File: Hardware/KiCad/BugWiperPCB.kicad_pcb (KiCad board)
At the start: 2 copper layers, 110 x 40 mm, 88 parts, among them J1 UJ20-C-H-G-SMT-1-P16-TR, J2 TBLH10-350-06BK, J3 Phoenix_1776508, J4 RJ45, J5 Conn_TagConnect_TC2030-NL_ESP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, Q1 NMOS_SO-8, U1 ESP32-S3-WROOM-1, U2 BTN9960LV, U3 BTN9960LV, U4 INA180A2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

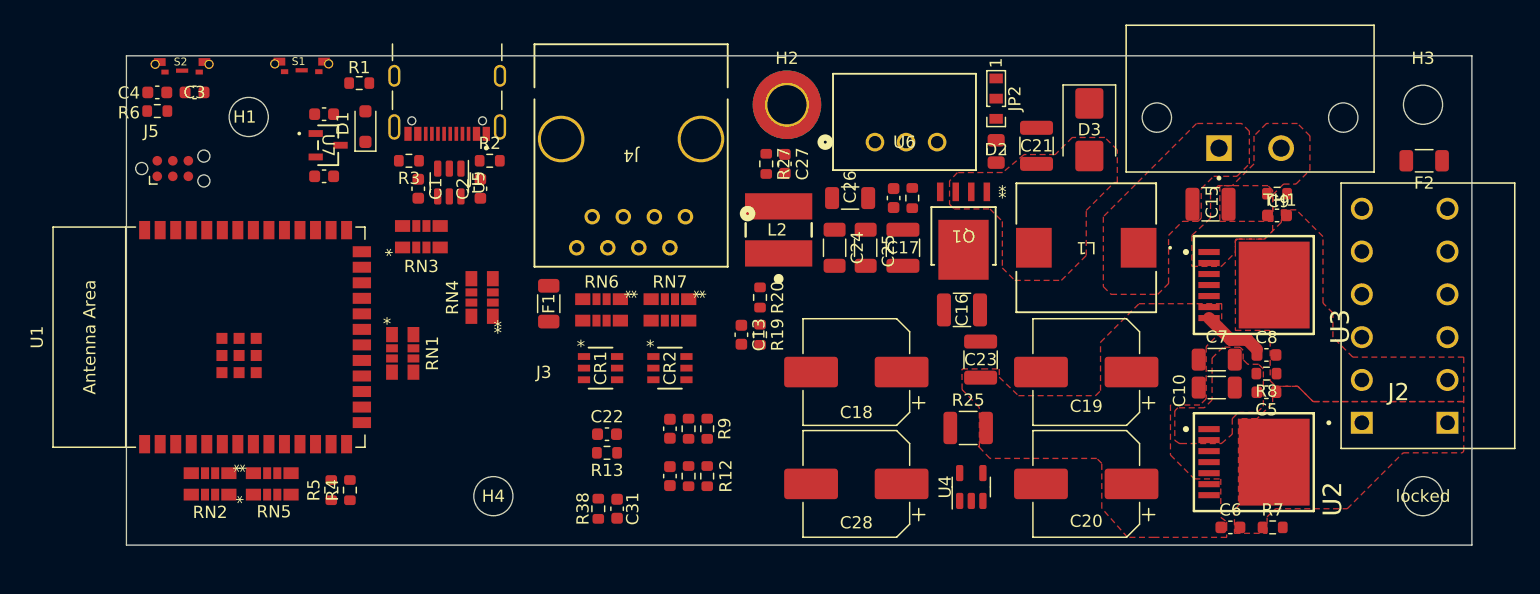
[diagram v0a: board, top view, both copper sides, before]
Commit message: update PCB, routing and Connector
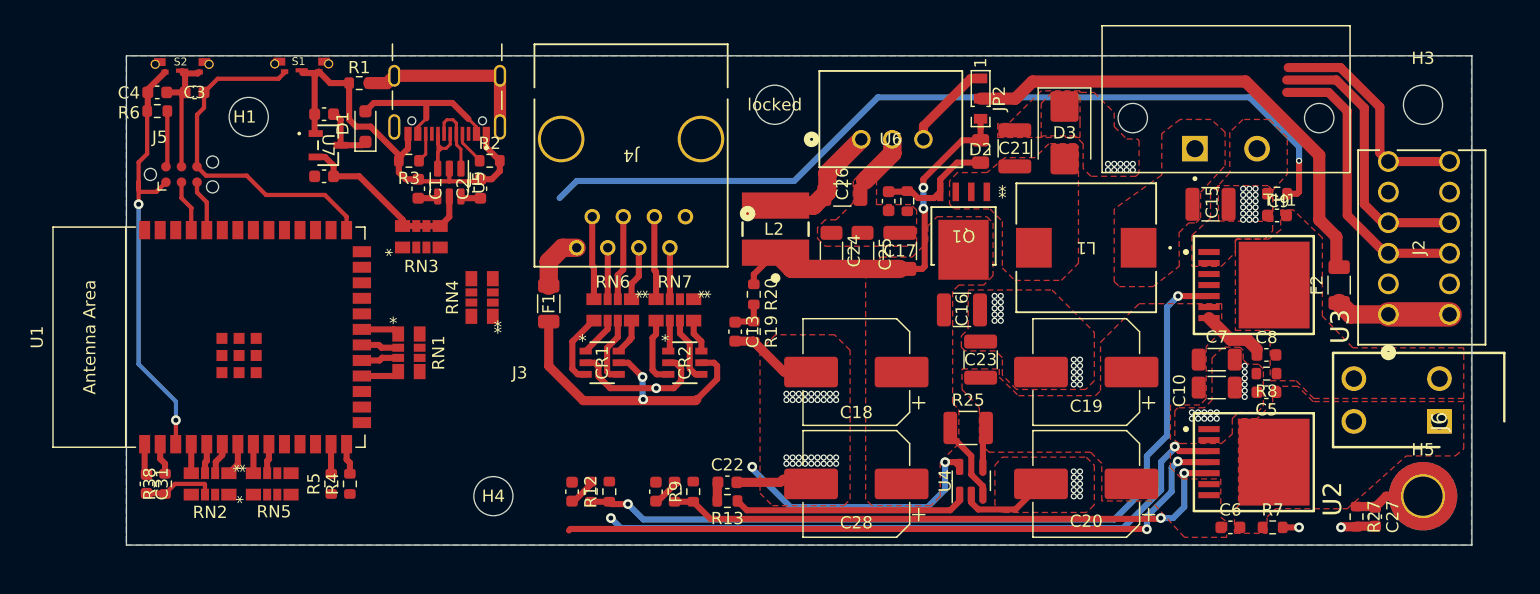
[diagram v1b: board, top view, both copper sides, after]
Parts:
- added J6: 1824420000, BugWiper_lib:SHDR4W80P700X350_2X2_770X1400X850P, F.Cu at (217.3, 89.9)
- J2: value TBLH10-350-06BK -> 1770924; footprint TBLH10_350_06BK-2:CUI_TBLH10-350-06BK -> BugWiper_lib:CONN_1814537
- moved locked 61.9 mm to (163.0, 64.0)
- moved H5 61.1 mm to (216.0, 96.0)
- moved C27 56.2 mm to (212.1, 97.7)
- moved R27 56.2 mm to (210.6, 97.7)
- moved C31 38.5 mm to (111.6, 95.0)
- moved R38 35.5 mm to (113.2, 95.0)
- moved J2 21.1 mm to (218.2, 70.2)
- moved F2 12.3 mm to (209.1, 78.7), turned to 90 degrees
- moved C22 10.6 mm to (159.1, 94.9)
- moved R13 10.6 mm to (159.1, 96.4)
- moved C12 8.10 mm to (146.4, 95.6)
- moved R11 8.10 mm to (148.0, 95.6), turned to -90 degrees
- moved R12 8.10 mm to (149.5, 95.6), turned to 90 degrees
- moved C11 5.27 mm to (153.3, 95.6)
- moved R10 5.27 mm to (154.8, 95.6), turned to -90 degrees
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- renumbered H2 to H5
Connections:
- C5 pad 1: Motor+ -> /Power/Motor+
- C6 pad 2: Motor+ -> /Power/Motor+
- C8 pad 2: Motor- -> /Power/Motor-
- C9 pad 1: Motor- -> /Power/Motor-
- F2 pad 1: Net-(J2-3) -> Net-(F2-Pad1)
- R7 pad 1: Motor+ -> /Power/Motor+
- R8 pad 1: Motor- -> /Power/Motor-
- RN1 pad 1: /ESP32-S3/M_IHN2 -> M__INH2
- RN1 pad 2: /ESP32-S3/M_INH1 -> M__INH1
- RN1 pad 3: /ESP32-S3/M_IN2 -> M__IN2
- RN1 pad 4: /ESP32-S3/M_IN1 -> M__IN1
- RN1 pad 5: M__IN1 -> /ESP32-S3/M_IN1
- RN1 pad 6: M__IN2 -> /ESP32-S3/M_IN2
- RN1 pad 7: M__INH1 -> /ESP32-S3/M_INH1
- RN1 pad 8: M__INH2 -> /ESP32-S3/M_IHN2
- U2 pad 8: Motor+ -> /Power/Motor+
- U3 pad 8: Motor- -> /Power/Motor-
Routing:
- net GND: track 0.00 -> 89.3 mm, vias 0 -> 113
- net +3.3V: track 0.00 -> 78.3 mm, vias 0 -> 4
- net /ESP32-S3/ADC_NTC: track 0.00 -> 76.3 mm, vias 0 -> 1
- net Net-(U3-IS): track 0.00 -> 66.4 mm, vias 0 -> 2
- net /ESP32-S3/M_INH1: track 0.00 -> 56.5 mm, vias 0 -> 2
- net /ESP32-S3/M_IN1: track 0.00 -> 53.6 mm, vias 0 -> 2
- net Net-(U2-IS): track 0.00 -> 47.4 mm, vias 0 -> 2
- net Net-(JP2-C): track 0.00 -> 40.7 mm
- net +12V: track 0.00 -> 38.1 mm, vias 0 -> 2
- net EN: track 0.00 -> 35.9 mm, vias 0 -> 2
- net Boot: track 0.00 -> 28.7 mm
- net EN_C2: track 0.00 -> 23.8 mm
- net EN_C1: track 0.00 -> 22.8 mm
- net /ESP32-S3/ADC_INA: track 0.00 -> 18.8 mm
- net switsch: track 0.00 -> 18.6 mm
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- added copper zone on F.Cu, net +12V
- added copper zone on F.Cu, net /Power/Motor+
- added copper zone on F.Cu, net /Power/Motor-
- added copper zone on B.Cu, net GND
- removed copper zone on F.Cu, net Motor+
- removed copper zone on F.Cu, net Motor-

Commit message: update PCB
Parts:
- U1: footprint PCM_Espressif:ESP32-S3-WROOM-1 -> BugWiper_lib:ESP32-S3-WROOM-1

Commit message: turn the esp32 90°
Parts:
- removed RN3: 47k_Pack04, BugWiper_lib:BO_CAY16
- moved C29 35.3 mm to (154.5, 90.9), turned to -90 degrees
- moved C30 35.0 mm to (149.5, 90.9), turned to -90 degrees
- moved U7 34.5 mm to (152.0, 90.6), turned to 0 degrees
- moved C31 27.9 mm to (139.3, 92.0), turned to 180 degrees
- moved H4 26.7 mm to (114.0, 90.0)
- moved R38 26.6 mm to (139.3, 90.5), turned to 0 degrees
- moved R5 24.1 mm to (140.0, 74.8), turned to -90 degrees
- moved RN2 23.9 mm to (139.3, 86.8), turned to 0 degrees
- moved R4 22.6 mm to (138.5, 74.8), turned to -90 degrees
- moved RN5 21.9 mm to (139.3, 81.7), turned to 180 degrees
- moved RN4 20.5 mm to (123.5, 66.5), turned to -90 degrees
- moved D1 15.2 mm to (141.8, 74.7)
- moved RN1 13.9 mm to (128.6, 71.1), turned to 90 degrees
- moved J5 11.9 mm to (113.7, 81.5), turned to 90 degrees
- moved C3 11.6 mm to (114.8, 74.6), turned to 90 degrees
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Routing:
- net +3.3V: track 78.3 -> 39.5 mm, vias 4 -> 3
- net EN: track 35.9 -> 3.75 mm, vias 2 -> 1
- net Boot: track 28.7 -> 0.00 mm
- net GND: track 89.3 -> 64.4 mm
- net Net-(D1-A): track 13.6 -> 8.29 mm
- net TX: track 4.26 -> 0.00 mm
- net RX: track 4.25 -> 0.00 mm
- net Net-(C1-Pad2): track 1.65 -> 5.84 mm
- net Net-(C2-Pad1): track 1.65 -> 4.04 mm
- net Net-(J1-SHIELD-PadSH1): track 15.1 -> 12.8 mm
- net +5V: track 4.99 -> 2.84 mm
- net D-: track 2.43 -> 4.38 mm
- net Net-(F1-Pad2): track 4.74 -> 3.43 mm
- net M__INH2: track 3.13 -> 2.59 mm
- net M__INH1: track 3.06 -> 2.53 mm
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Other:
- outline, holes or cut-outs redrawn

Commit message: routing
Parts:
- added C32: 10nF, Capacitor_SMD:C_0603_1608Metric, F.Cu at (124.7, 70.2)
- added C33: 10nF, Capacitor_SMD:C_0603_1608Metric, F.Cu at (124.7, 71.8)
- added C34: 10nF, Capacitor_SMD:C_0603_1608Metric, F.Cu at (120.3, 71.8)
- added C35: 10nF, Capacitor_SMD:C_0603_1608Metric, F.Cu at (120.3, 70.2)
- added C36: 10nF, Capacitor_SMD:C_0603_1608Metric, F.Cu at (141.0, 84.1)
- added C37: 10nF, Capacitor_SMD:C_0603_1608Metric, F.Cu at (138.4, 83.3)
- added C38: 10nF, Capacitor_SMD:C_0603_1608Metric, F.Cu at (154.7, 91.3)
- added R14: 1k, Resistor_SMD:R_0603_1608Metric, F.Cu at (142.6, 86.7)
- D1: value 1N5819WS -> locked
- moved TH1 26.9 mm to (209.0, 97.7), turned to -90 degrees
- moved C30 4.48 mm to (145.0, 90.2)
- moved C29 4.11 mm to (150.5, 90.2), turned to 90 degrees
- moved U7 3.74 mm to (148.3, 90.2)
- moved R19 3.08 mm to (158.7, 80.9), turned to 90 degrees
- moved R2 2.12 mm to (140.6, 70.9), turned to -90 degrees
- moved R3 2.12 mm to (132.5, 70.9), turned to -90 degrees
- moved RN5 1.83 mm to (141.0, 80.9)
- moved C13 1.73 mm to (160.3, 80.9), turned to 90 degrees
- moved R20 1.51 mm to (161.9, 80.9)
- moved S2 1.49 mm to (119.3, 60.0)
- moved RN4 1.42 mm to (122.6, 67.6)
- moved C16 0.91 mm to (178.1, 81.7)
- moved C23 0.77 mm to (180.0, 85.6)
- moved CR1 0.70 mm to (149.6, 85.1)
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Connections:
- net switsch renamed sw_1
- RN5 pad 3: unconnected-(RN5-R3.1-Pad3) -> Net-(RN5-R3.1)
- RN5 pad 6: unconnected-(RN5-R3.2-Pad6) -> SW1
- U1 pad 10: unconnected-(U1-GPIO17/U1TXD/ADC2_CH6-Pad10) -> SW1
- U1 pad 11: unconnected-(U1-GPIO18/U1RXD/ADC2_CH7/CLK_OUT3-Pad11) -> OUT1
- U1 pad 12: OUT1 -> OUT2
- U1 pad 17: OUT2 -> unconnected-(U1-GPIO9/TOUCH9/ADC1_CH8/FSPIHD/SUBSPIHD-Pad17)
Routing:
- net +3.3V: track 39.5 -> 166.5 mm, vias 3 -> 9
- net /ESP32-S3/M_IHN2: track 0.00 -> 86.9 mm, vias 0 -> 8
- net /ESP32-S3/M_IN2: track 0.00 -> 85.6 mm, vias 0 -> 6
- net EN_C2: track 23.8 -> 86.1 mm, vias 0 -> 8
- net EN_C1: track 22.8 -> 83.9 mm, vias 0 -> 4
- net EN: track 3.75 -> 58.5 mm, vias 1 -> 2
- net sw_1: track 18.6 -> 70.6 mm, vias 0 -> 2
- net Boot: track 0.00 -> 30.0 mm
- net GND: track 64.4 -> 76.8 mm, vias 113 -> 146
- net IN_4: track 0.00 -> 10.2 mm, vias 0 -> 2
- net RX: track 0.00 -> 9.52 mm
- net TX: track 0.00 -> 9.52 mm
- net IN_1: track 0.00 -> 8.97 mm, vias 0 -> 2
- net /ESP32-S3/M_INH1: track 56.5 -> 47.6 mm
- net IN_3: track 0.00 -> 8.23 mm
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
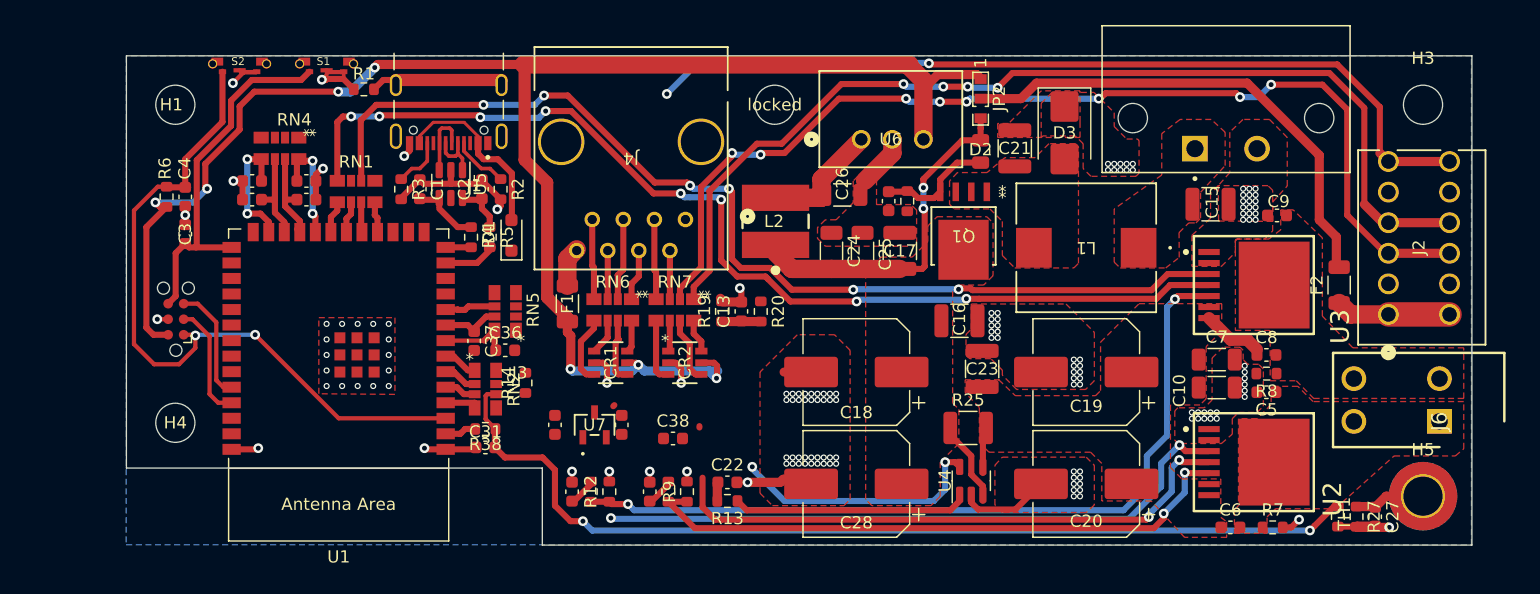
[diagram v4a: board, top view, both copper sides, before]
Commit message: routing and change to 4 layer PCB
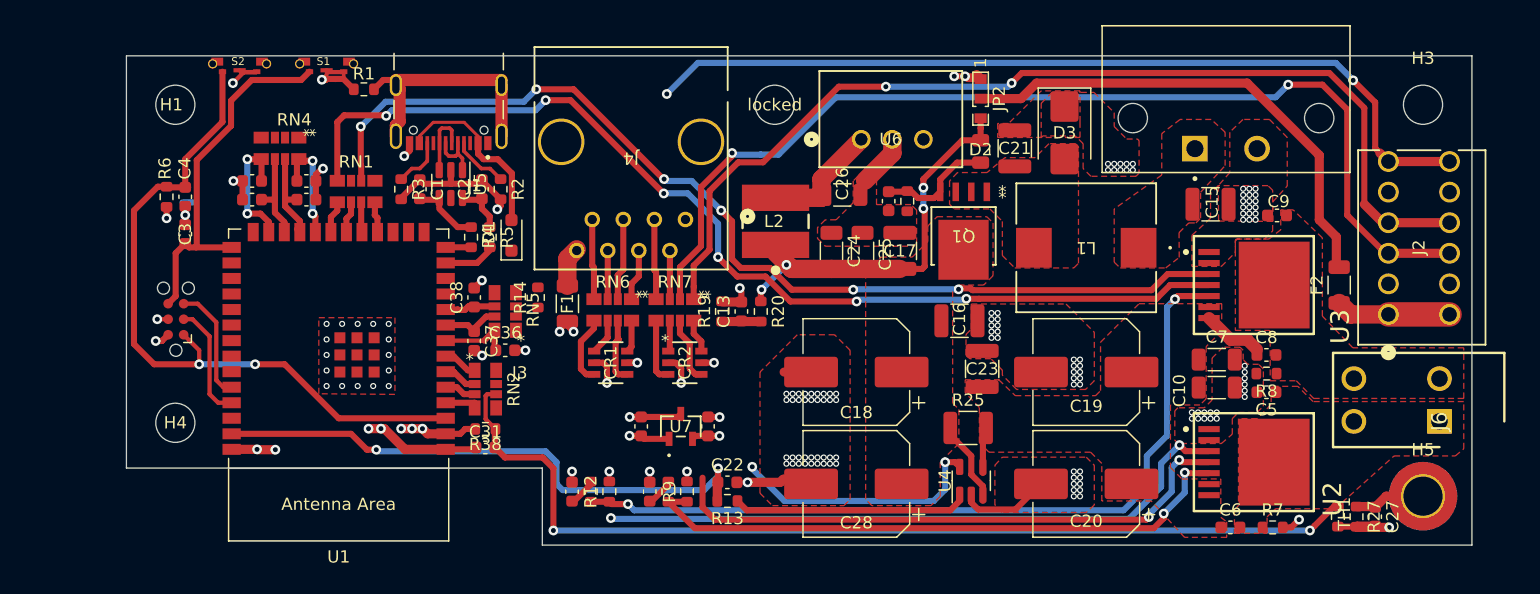
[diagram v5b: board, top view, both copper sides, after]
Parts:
- moved C38 19.9 mm to (138.4, 79.8), turned to 90 degrees
- moved R14 7.06 mm to (143.6, 79.8)
- moved C30 7.05 mm to (152.1, 90.3)
- moved C29 7.05 mm to (157.5, 90.3)
- moved U7 7.05 mm to (155.3, 90.3)
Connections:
- R14 pad 2: /ESP32-S3/sw_1 -> sw_1
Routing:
- net +3.3V: track 166.5 -> 40.8 mm, vias 9 -> 14
- net A_INA: track 1.54 -> 46.5 mm, vias 0 -> 2
- net GND: track 76.8 -> 90.1 mm, vias 146 -> 153
- net Net-(J1-SHIELD-PadSH1): track 10.7 -> 19.4 mm
- net +5V: track 0.24 -> 4.30 mm, vias 0 -> 1
- net +12V: track 34.8 -> 38.7 mm, vias 2 -> 4
- net /ESP32-S3/M_IN2: track 85.6 -> 84.3 mm
- net /ESP32-S3/ADC_NTC: track 79.7 -> 81.0 mm
- net /ESP32-S3/M_IHN2: track 86.9 -> 86.0 mm, vias 8 -> 6
- net EN: track 58.5 -> 57.8 mm
- net EN_C2: track 86.1 -> 85.6 mm, vias 8 -> 2
- net EN_C1: track 83.9 -> 83.6 mm, vias 4 -> 2
- added copper zone on In2.Cu, net +3.3V
- added copper zone on In1.Cu, net GND
- removed copper zone on B.Cu, net GND
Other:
- copper layers 2 -> 4

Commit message: Update BugWiperPCB.kicad_pcb
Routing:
- net +3.3V: track 40.8 -> 39.9 mm
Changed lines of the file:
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@@
   (segment (start 175.9966 96.393) (end 176.9364 95.4532) (width 0.5) (layer "B.Cu") (net 47))
   (segment (start 163.795657 96.393) (end 175.9966 96.393) (width 0.5) (layer "B.Cu") (net 47))
-  (segment (start 114.577492 71.985508) (end 115.466492 71.985508) (width 0.5) (layer "B.Cu") (net 47))
   (segment (start 146.812 75.819) (end 146.05 76.581) (width 1.5) (layer "F.Cu") (net 48))
   (segment locked (start 146.05 76.581) (end 146.05 78.8015) (width 1.5) (layer "F.Cu") (net 48))

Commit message: PCB mostly finished
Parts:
- added C39: 100nF, Capacitor_SMD:C_0603_1608Metric, F.Cu at (138.9, 77.5)
- added CR3: D5V0P4UR6SO-7, BugWiper_lib:SOT26_DIO, F.Cu at (154.4, 85.0)
- added R15: 1k, Resistor_SMD:R_0603_1608Metric, F.Cu at (150.4, 88.2)
- added RN3: 100R_Pack04, BugWiper_lib:BO_CAY16, F.Cu at (154.2, 81.2)
- C38: value 10nF -> 100nF
- moved C29 48.3 mm to (113.2, 71.2), turned to 180 degrees
- moved U7 45.6 mm to (112.8, 73.9), turned to 90 degrees
- moved C30 41.6 mm to (112.8, 76.6), turned to 0 degrees
- moved D1 25.7 mm to (115.8, 73.9)
- moved R14 13.3 mm to (153.9, 88.2), turned to 180 degrees
- moved C13 11.3 mm to (160.5, 92.2)
- moved R19 11.3 mm to (158.9, 92.2)
- moved R20 11.3 mm to (162.1, 92.2)
- moved F1 6.02 mm to (141.7, 76.1), turned to -90 degrees
- moved C3 5.65 mm to (115.4, 69.0)
- moved RN7 5.20 mm to (160.0, 81.2)
- moved CR2 4.37 mm to (160.0, 85.0)
- moved C4 3.52 mm to (112.4, 69.0)
- moved R6 2.64 mm to (113.9, 69.0)
- moved RN6 1.38 mm to (148.4, 81.2)
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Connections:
- CR2 pad 1: OUT_1 -> Net-(CR2-IO_1)
- CR2 pad 3: OUT_2 -> Net-(CR2-IO_2)
- J4 pad 2: Net-(RN7C-R3.1) -> Net-(RN3C-R3.1)
- J4 pad 3: Net-(RN7D-R4.1) -> Net-(RN3D-R4.1)
- R14 pad 1: Net-(RN5-R3.1) -> OUT_1
- R14 pad 2: sw_1 -> OUT1
- RN5 pad 3: Net-(RN5-R3.1) -> Net-(CR2-IO_1)
- RN5 pad 4: unconnected-(RN5-R4.1-Pad4) -> Net-(CR2-IO_2)
- RN5 pad 5: unconnected-(RN5-R4.2-Pad5) -> SW2
- RN7 pad 1: EN_C1 -> /ESP32-S3/sw_2
- RN7 pad 2: EN_C2 -> EN_C1
- RN7 pad 3: Net-(RN7C-R3.1) -> EN_C2
- RN7 pad 4: Net-(RN7D-R4.1) -> sw_1
- RN7 pad 5: OUT_2 -> Net-(CR2-IO_2)
- RN7 pad 6: OUT_1 -> Net-(CR2-IO_1)
- U1 pad 11: OUT1 -> SW2
- U1 pad 17: unconnected-(U1-GPIO9/TOUCH9/ADC1_CH8/FSPIHD/SUBSPIHD-Pad17) -> OUT1
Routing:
- net /ESP32-S3/M_INH1: track 47.6 -> 107.5 mm, vias 2 -> 6
- net /ESP32-S3/M_IN1: track 52.7 -> 108.4 mm, vias 2 -> 4
- net Net-(CR1-IO_4): track 2.64 -> 52.4 mm, vias 0 -> 4
- net Net-(CR1-IO_2): track 5.71 -> 52.6 mm, vias 0 -> 4
- net Net-(CR1-IO_1): track 2.95 -> 48.3 mm, vias 0 -> 4
- net Net-(CR1-IO_3): track 5.35 -> 49.3 mm, vias 0 -> 4
- net Net-(CR2-IO_4): track 2.75 -> 36.1 mm
- net Net-(CR2-IO_1): track 0.00 -> 31.0 mm, vias 0 -> 2
- net OUT1: track 0.00 -> 30.8 mm, vias 0 -> 2
- net Net-(CR2-IO_2): track 0.00 -> 30.0 mm
- net Net-(CR2-IO_3): track 5.40 -> 35.4 mm
- net OUT2: track 0.00 -> 25.6 mm, vias 0 -> 2
- net Net-(D1-A): track 14.9 -> 38.5 mm, vias 0 -> 2
- net /ESP32-S3/ADC_VBat: track 4.72 -> 25.1 mm, vias 0 -> 2
- net sw_1: track 70.6 -> 88.7 mm
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- added copper zone on B.Cu, net +12V
- added copper zone on In2.Cu, net +12V
- added copper zone on B.Cu, net +12V_HighSide
- added copper zone on In2.Cu, net +12V_HighSide
- added copper zone on B.Cu, net /Power/+VBat
- added copper zone on In2.Cu, net /Power/+VBat
- added copper zone on B.Cu, net /Power/+VBat*
- added copper zone on In2.Cu, net /Power/+VBat*
- added copper zone on B.Cu, net /Power/Motor+
- added copper zone on In1.Cu, net /Power/Motor+
- added copper zone on In2.Cu, net /Power/Motor+
- added copper zone on B.Cu, net /Power/Motor-
- added copper zone on In1.Cu, net /Power/Motor-
- added copper zone on In2.Cu, net /Power/Motor-
- added copper zone on B.Cu, net GND
- added copper zone on In2.Cu, net GND
